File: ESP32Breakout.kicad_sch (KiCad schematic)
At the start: 7 parts, among them J1 PIN6-9_Breakout, J2 PIN10-13_Breakout, U1 ESP32-S3

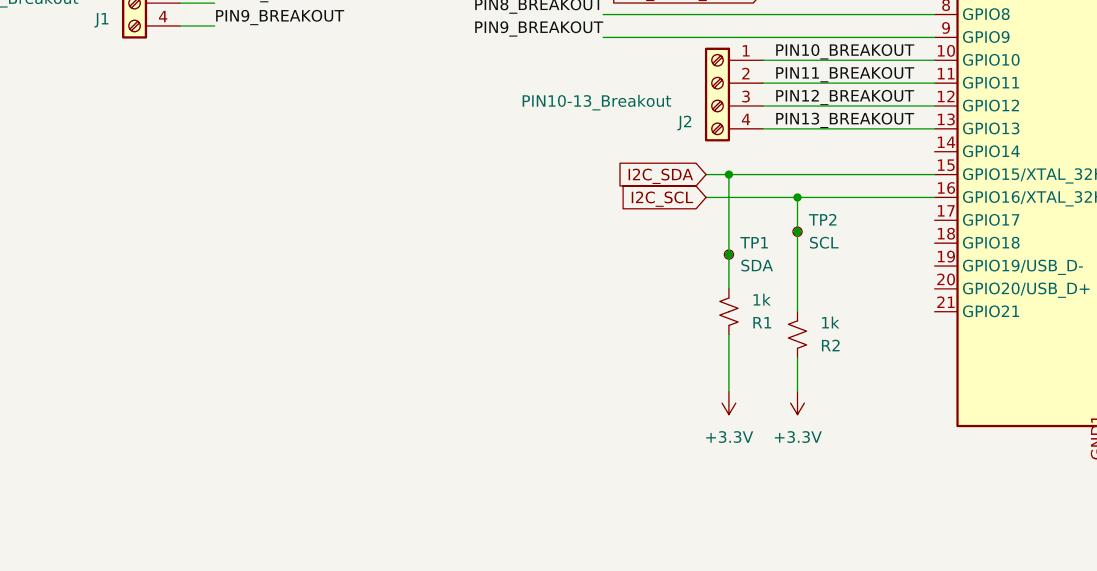
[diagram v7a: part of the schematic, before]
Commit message: Add current sensing and fuse mount for IGN
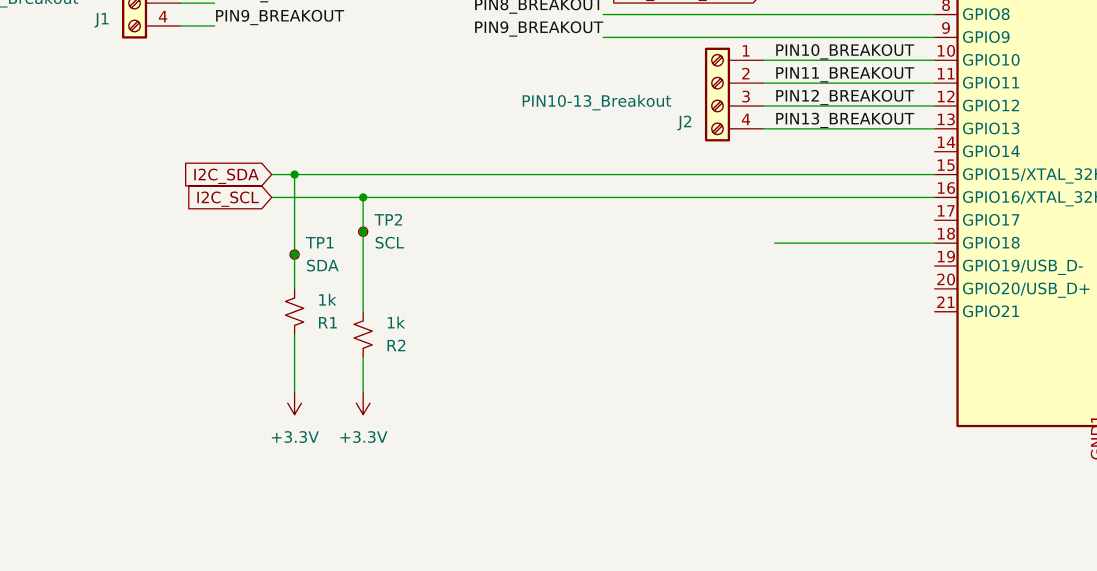
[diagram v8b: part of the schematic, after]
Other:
- moved on the sheet: R1, R2, TP1, TP2
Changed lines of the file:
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@@
 	)
 	(junction
-		(at 96.52 97.79)
+		(at 48.26 97.79)
 		(diameter 0)
 		(color 0 0 0 0)
 	)
 	(junction
-		(at 96.52 88.9)
+		(at 48.26 88.9)
 		(diameter 0)
 		(color 0 0 0 0)
@@
 	)
 	(junction
-		(at 104.14 95.25)
+		(at 55.88 95.25)
 		(diameter 0)
 		(color 0 0 0 0)
 	)
 	(junction
-		(at 104.14 91.44)
+		(at 55.88 91.44)
 		(diameter 0)
 		(color 0 0 0 0)
@@
 	(wire
 		(pts
-			(xy 104.14 91.44) (xy 104.14 95.25)
+			(xy 55.88 91.44) (xy 55.88 95.25)
 		)
 		(stroke
@@
 	(wire
 		(pts
-			(xy 96.52 106.68) (xy 96.52 113.03)
+			(xy 48.26 106.68) (xy 48.26 113.03)
 		)
 		(stroke
@@
 	(wire
 		(pts
-			(xy 104.14 95.25) (xy 104.14 104.14)
+			(xy 55.88 95.25) (xy 55.88 104.14)
 		)
 		(stroke
@@
 	(wire
 		(pts
-			(xy 96.52 101.6) (xy 96.52 97.79)
+			(xy 48.26 101.6) (xy 48.26 97.79)
 		)
 		(stroke
@@
 	(wire
 		(pts
-			(xy 93.98 91.44) (xy 104.14 91.44)
+			(xy 45.72 91.44) (xy 55.88 91.44)
 		)
 		(stroke
@@
 	(wire
 		(pts
-			(xy 96.52 88.9) (xy 119.38 88.9)
+			(xy 48.26 88.9) (xy 119.38 88.9)
 		)
 		(stroke
@@
 	(wire
 		(pts
-			(xy 93.98 88.9) (xy 96.52 88.9)
+			(xy 101.6 96.52) (xy 119.38 96.52)
+		)
+		(stroke
+			(width 0)
+			(type default)
+		)
+	)
+	(wire
+		(pts
+			(xy 45.72 88.9) (xy 48.26 88.9)
 		)
 		(stroke
@@
 	(wire
 		(pts
-			(xy 96.52 97.79) (xy 96.52 88.9)
+			(xy 48.26 97.79) (xy 48.26 88.9)
 		)
 		(stroke
@@
 	(wire
 		(pts
-			(xy 104.14 91.44) (xy 119.38 91.44)
+			(xy 55.88 91.44) (xy 119.38 91.44)
 		)
 		(stroke
@@
 	(wire
 		(pts
-			(xy 104.14 109.22) (xy 104.14 113.03)
+			(xy 55.88 109.22) (xy 55.88 113.03)
 		)
 		(stroke
@@
 	(global_label "I2C_SCL"
 		(shape input)
-		(at 93.98 91.44 180)
+		(at 45.72 91.44 180)
 		(fields_autoplaced yes)
 		(effects
@@
 		)
 		(property "Intersheetrefs" "${INTERSHEET_REFS}"
-			(at 83.4353 91.44 0)
+			(at 35.1753 91.44 0)
 			(effects
 				(font
@@
 	(global_label "I2C_SDA"
 		(shape input)
-		(at 93.98 88.9 180)
+		(at 45.72 88.9 180)
 		(fields_autoplaced yes)
 		(effects
@@
 		)
 		(property "Intersheetrefs" "${INTERSHEET_REFS}"
-			(at 83.3748 88.9 0)
+			(at 35.1148 88.9 0)
 			(effects
 				(font
@@
 	(symbol
 		(lib_id "power:+3.3V")
-		(at 96.52 113.03 0)
+		(at 48.26 113.03 0)
 		(mirror x)
 		(unit 1)
@@
 		(fields_autoplaced yes)
 		(property "Reference" "#PWR01"
-			(at 96.52 109.22 0)
+			(at 48.26 109.22 0)
 			(effects
 				(font
@@
 		)
 		(property "Value" "+3.3V"
-			(at 96.52 118.11 0)
+			(at 48.26 118.11 0)
 			(effects
 				(font
@@
 		)
 		(property "Footprint" ""
-			(at 96.52 113.03 0)
+			(at 48.26 113.03 0)
 			(effects
 				(font
@@
 		)
 		(property "Datasheet" ""
-			(at 96.52 113.03 0)
+			(at 48.26 113.03 0)
 			(effects
 				(font
@@
 		)
 		(property "Description" "Power symbol creates a global label with name \"+3.3V\""
-			(at 96.52 113.03 0)
+			(at 48.26 113.03 0)
 			(effects
 				(font
@@
 	(symbol
 		(lib_id "Connector:TestPoint_Small")
-		(at 104.14 95.25 0)
+		(at 55.88 95.25 0)
 		(unit 1)
 		(exclude_from_sim no)
@@
 		(fields_autoplaced yes)
 		(property "Reference" "TP2"
-			(at 105.41 93.9799 0)
+			(at 57.15 93.9799 0)
 			(effects
 				(font
@@
 		)
 		(property "Value" "SCL"
-			(at 105.41 96.5199 0)
+			(at 57.15 96.5199 0)
 			(effects
 				(font
@@
 		)
 		(property "Footprint" "TestPoint:TestPoint_Pad_D1.5mm"
-			(at 109.22 95.25 0)
+			(at 60.96 95.25 0)
 			(effects
 				(font
@@
 		)
 		(property "Datasheet" "~"
-			(at 109.22 95.25 0)
+			(at 60.96 95.25 0)
 			(effects
 				(font
@@
 		)
 		(property "Description" "test point"
-			(at 104.14 95.25 0)
+			(at 55.88 95.25 0)
 			(effects
 				(font
@@
 	(symbol
 		(lib_id "power:+3.3V")
-		(at 104.14 113.03 0)
+		(at 55.88 113.03 0)
 		(mirror x)
 		(unit 1)
@@
 		(fields_autoplaced yes)
 		(property "Reference" "#PWR02"
-			(at 104.14 109.22 0)
+			(at 55.88 109.22 0)
 			(effects
 				(font
@@
 		)
 		(property "Value" "+3.3V"
-			(at 104.14 118.11 0)
+			(at 55.88 118.11 0)
 			(effects
 				(font
@@
 		)
 		(property "Footprint" ""
-			(at 104.14 113.03 0)
+			(at 55.88 113.03 0)
 			(effects
 				(font
@@
 		)
 		(property "Datasheet" ""
-			(at 104.14 113.03 0)
+			(at 55.88 113.03 0)
 			(effects
 				(font
@@
 		)
 		(property "Description" "Power symbol creates a global label with name \"+3.3V\""
-			(at 104.14 113.03 0)
+			(at 55.88 113.03 0)
 			(effects
 				(font
@@
 	(symbol
 		(lib_id "Connector:TestPoint_Small")
-		(at 96.52 97.79 0)
+		(at 48.26 97.79 0)
 		(unit 1)
 		(exclude_from_sim no)
@@
 		(fields_autoplaced yes)
 		(property "Reference" "TP1"
-			(at 97.79 96.5199 0)
+			(at 49.53 96.5199 0)
 			(effects
 				(font
@@
 		)
 		(property "Value" "SDA"
-			(at 97.79 99.0599 0)
+			(at 49.53 99.0599 0)
 			(effects
 				(font
@@
 		)
 		(property "Footprint" "TestPoint:TestPoint_Pad_D1.5mm"
-			(at 101.6 97.79 0)
+			(at 53.34 97.79 0)
 			(effects
 				(font
@@
 		)
 		(property "Datasheet" "~"
-			(at 101.6 97.79 0)
+			(at 53.34 97.79 0)
 			(effects
 				(font
@@
 		)
 		(property "Description" "test point"
-			(at 96.52 97.79 0)
+			(at 48.26 97.79 0)
 			(effects
 				(font
@@
 	(symbol
 		(lib_id "Device:R_Small_US")
-		(at 104.14 106.68 0)
+		(at 55.88 106.68 0)
 		(mirror x)
 		(unit 1)
@@
 		(fields_autoplaced yes)
 		(property "Reference" "R2"
-			(at 106.68 107.9501 0)
+			(at 58.42 107.9501 0)
 			(effects
 				(font
@@
 		)
 		(property "Value" "1k"
-			(at 106.68 105.4101 0)
+			(at 58.42 105.4101 0)
 			(effects
 				(font
@@
 		)
 		(property "Footprint" "Resistor_SMD:R_0402_1005Metric"
-			(at 104.14 106.68 0)
+			(at 55.88 106.68 0)
 			(effects
 				(font
@@
 		)
 		(property "Datasheet" "~"
-			(at 104.14 106.68 0)
+			(at 55.88 106.68 0)
 			(effects
 				(font
@@
 		)
 		(property "Description" "Resistor, small US symbol"
-			(at 104.14 106.68 0)
+			(at 55.88 106.68 0)
 			(effects
 				(font
@@
 	(symbol
 		(lib_id "Device:R_Small_US")
-		(at 96.52 104.14 0)
+		(at 48.26 104.14 0)
 		(mirror x)
 		(unit 1)
@@
 		(fields_autoplaced yes)
 		(property "Reference" "R1"
-			(at 99.06 105.4101 0)
+			(at 50.8 105.4101 0)
 			(effects
 				(font
@@
 		)
 		(property "Value" "1k"
-			(at 99.06 102.8701 0)
+			(at 50.8 102.8701 0)
 			(effects
 				(font
@@
 		)
 		(property "Footprint" "Resistor_SMD:R_0402_1005Metric"
-			(at 96.52 104.14 0)
+			(at 48.26 104.14 0)
 			(effects
 				(font
@@
 		)
 		(property "Datasheet" "~"
-			(at 96.52 104.14 0)
+			(at 48.26 104.14 0)
 			(effects
 				(font
@@
 		)
 		(property "Description" "Resistor, small US symbol"
-			(at 96.52 104.14 0)
-			(effects
-				(font
+			(at 48.26 104.14 0)
+			(effects
+				(font
